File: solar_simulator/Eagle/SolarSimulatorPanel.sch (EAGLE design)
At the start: 131 parts, among them J1 DCJ0202, J2 DCJ0202

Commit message: rev 2.1 of solar simulator
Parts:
- removed R28: 220, oresat-rcl:R-US_0402-A-NOSILK
- removed U$5: AP2127, U-Diodes-AP2127-LDO:AP2127
- added C13, C14, C15: 10u, rcl:C-EUC2220K
- added TP27, TP28, TP29, TP30: TEST-POINT, Tova:TEST-POINT
- BLUE1, BLUE10, BLUE11, BLUE12, BLUE13, BLUE14, BLUE15, BLUE2, BLUE3, BLUE4, BLUE5, BLUE6, BLUE7, BLUE8: DIS (none) -> Digi-Key; DPN (none) -> XQEROY-00-0000-000000L01CT-ND; MFR (none) -> Cree; MPN (none) -> XQEROY-00-0000-000000L01
- BLUE9: DIS (none) -> Digi-Key; DPM (none) -> XQEROY-00-0000-000000L01CT-ND; MFR (none) -> Cree; MPN (none) -> XQEROY-00-0000-000000L01
- C1: value .1 u -> 100n
- C12, C2, C4, C5, C6: value .1u -> 100n
- C7, C8, C9: value .15u -> 150n; device oresat-rcl:C-EU0402-A-NOSILK -> rcl:C-EUC0805K
- GREE9, GREEN10, GREEN11, GREEN12, GREEN15, GREEN4, GREEN5, GREEN6, GREEN7, GREEN8: DIS (none) -> Digi-Key; DPN (none) -> XQEGRN-00-0000-000000D03CT-ND; MFR (none) -> Cree; MPN (none) -> XQEGRN-00-0000-000000D03
- GREEN1: DIS (none) -> Digi-Key; DPN (none) -> XQEGRN-00-0000-000000D03CT-ND; MFR (none) -> CREE; MPN (none) -> XQEGRN-00-0000-000000D03
- GREEN13: DIS (none) -> Digi-Key; DPN (none) -> XQEGRN-00-0000-000000D03CT-ND; MFR (none) -> Green; MPN (none) -> XQEGRN-00-0000-000000D03
- GREEN14, GREEN3: DIS (none) -> Digi-Key; DPN (none) -> XQEGRN-00-0000-000000D03CT-ND; MPN (none) -> XQEGRN-00-0000-000000D03
- GREEN2: DPN (none) -> XQEGRN-00-0000-000000D03CT-ND; MFR (none) -> Cree; MPN (none) -> XQEGRN-00-0000-000000D03
- J1: value DCJ0202 -> PJ-102B; device con-jack:DCJ0202 -> J-CUI-PJ102B-Barrel_Jack:PJ-102B; DIS (none) -> Digi-Key; DPN (none) -> 626-1968-ND; MFR (none) -> Conec
- J2: value DCJ0202 -> RAPC722BKZ-TH; device con-jack:DCJ0202 -> J-SwitchCraft-RAPC722BKZ-Barrel_Jack:RAPC722BKZ-TH; DIS (none) -> Digi-Key; DPN (none) -> SC3832-ND; MFR (none) -> SwitchCraft; MPN (none) -> RAPC722BKZ
- L1: DIS (none) -> Digi-Key; DPN (none) -> TE2201TR-ND; MPN (none) -> SH150S-1.02-168
- L2, L3: DIS (none) -> Digi-Key; DPN (none) -> TE2201TR-ND; MFR (none) -> Amgis; MPN (none) -> SH150S-1.02-168
- PCB1: device solarsim:ARDUINO_NANO -> U-Arduino-Nano-DevBoard:ARDUINO_NANO
- R1, R2: value 10k -> 4.7k
- R18, R19, R20: value TBD -> 300m; device oresat-rcl:R-US_0402-A-NOSILK -> rcl:R-US_R0805
- RED1, RED10, RED11, RED12, RED13, RED14, RED15, RED2, RED3, RED4, RED5, RED6, RED7, RED8, RED9: DIS (none) -> Digi-Key; DPN (none) -> XQERED-00-0000-000000701CT-ND; MFR (none) -> Cree; MPN (none) -> XQERED-00-0000-000000701
- RT1, RT2, RT3, RT4: device solarsim:NTCTHERMISTER -> R-Generic-Thermister0402:NTCTHERMISTER
- U$1, U$3: value TPS92512 -> (none); DIS (none) -> Digi-Key; DPN (none) -> 296-41002-1-ND; MFR (none) -> Texas Instruments; MPN (none) -> TPS92512DGQR
- U$2: value TPS92512 -> (none); DIS (none) -> Digi-key; DPN (none) -> 296-41002-1-ND; MFR (none) -> Texas Instruments; MPN (none) -> TPS92512DGQR
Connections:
- net N$1 renamed SDA
- net N$3 renamed SCL
- net N$32 renamed !LDAC
- net VCC renamed 12V
- removed net N$73: U$6.S, U$7.P$1
- removed net N$74: U$7.P$2, U$8.P$1
- removed net N$75: U$8.P$2, U$9.P$1
- removed net N$76: U$10.P$1, U$9.P$2
- removed net N$78: R28.1, R29.2, TP15.1, U$6.G
- removed net VCC/2: C4.1, C5.1, J2.3, R6.2, R8.2, TP12.1, U$2.VIN, U$3.VIN
- removed net VCC/3: C6.1, R10.2, U$1.VIN
- new net !RESET: PCB1.RESET, TP27.1
- new net 56V: C13.1, C14.1, C15.1, C4.1, C5.1, C6.1, J2.3, R10.2, R6.2, R8.2, TP12.1, U$1.VIN, U$2.VIN, U$3.VIN
- new net N$62: U$10.P$1, U$6.S, U$7.P$1, U$8.P$1, U$9.P$1
- new net N$84: TP30.1, U$3.PDIM
- new net N$85: TP28.1, U$2.PDIM
- new net N$86: TP29.1, U$1.PDIM
- net GND: now also C13.2, C14.2, C15.2, U$7.P$2, U$8.P$2, U$9.P$2; no longer U$5.GND
- net N$22: no longer C7.1
- net N$24: no longer C8.1
- net N$25: no longer C9.1
- net N$4: no longer TP16.1, U$5.VOUT
- net N$69: now also C9.1
- net N$70: now also C8.1
- net N$72: now also C7.1
- net N$79: now also R29.2, TP15.1, U$6.G; no longer R28.2
- net N$80: now also TP16.1, U$4.VOUTD; no longer U$5.!SHDN, U$5.VIN
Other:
- note added: "0805"
- note added: "NOTE: AREF bypassed on daughter board"
- note added: "NOTE: All resistors and capacitors are 0402 unless otherwise noted"
- note added: "NOTE: Switching Frequency is 1 MHz"
- note added: "TODO: Give Values to diode"
- note added: "TODO: Reference designator and value"
- note added: "TODO: add reference designator"
- note added: "TODO: extend board and add 4 mounting holes for solar panel. Use solar panel holes on top and bottom of board"
- moved on the sheet: C4, C5, C6, D1, D2, D3, J2, L1, L2, L3, R1, R2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

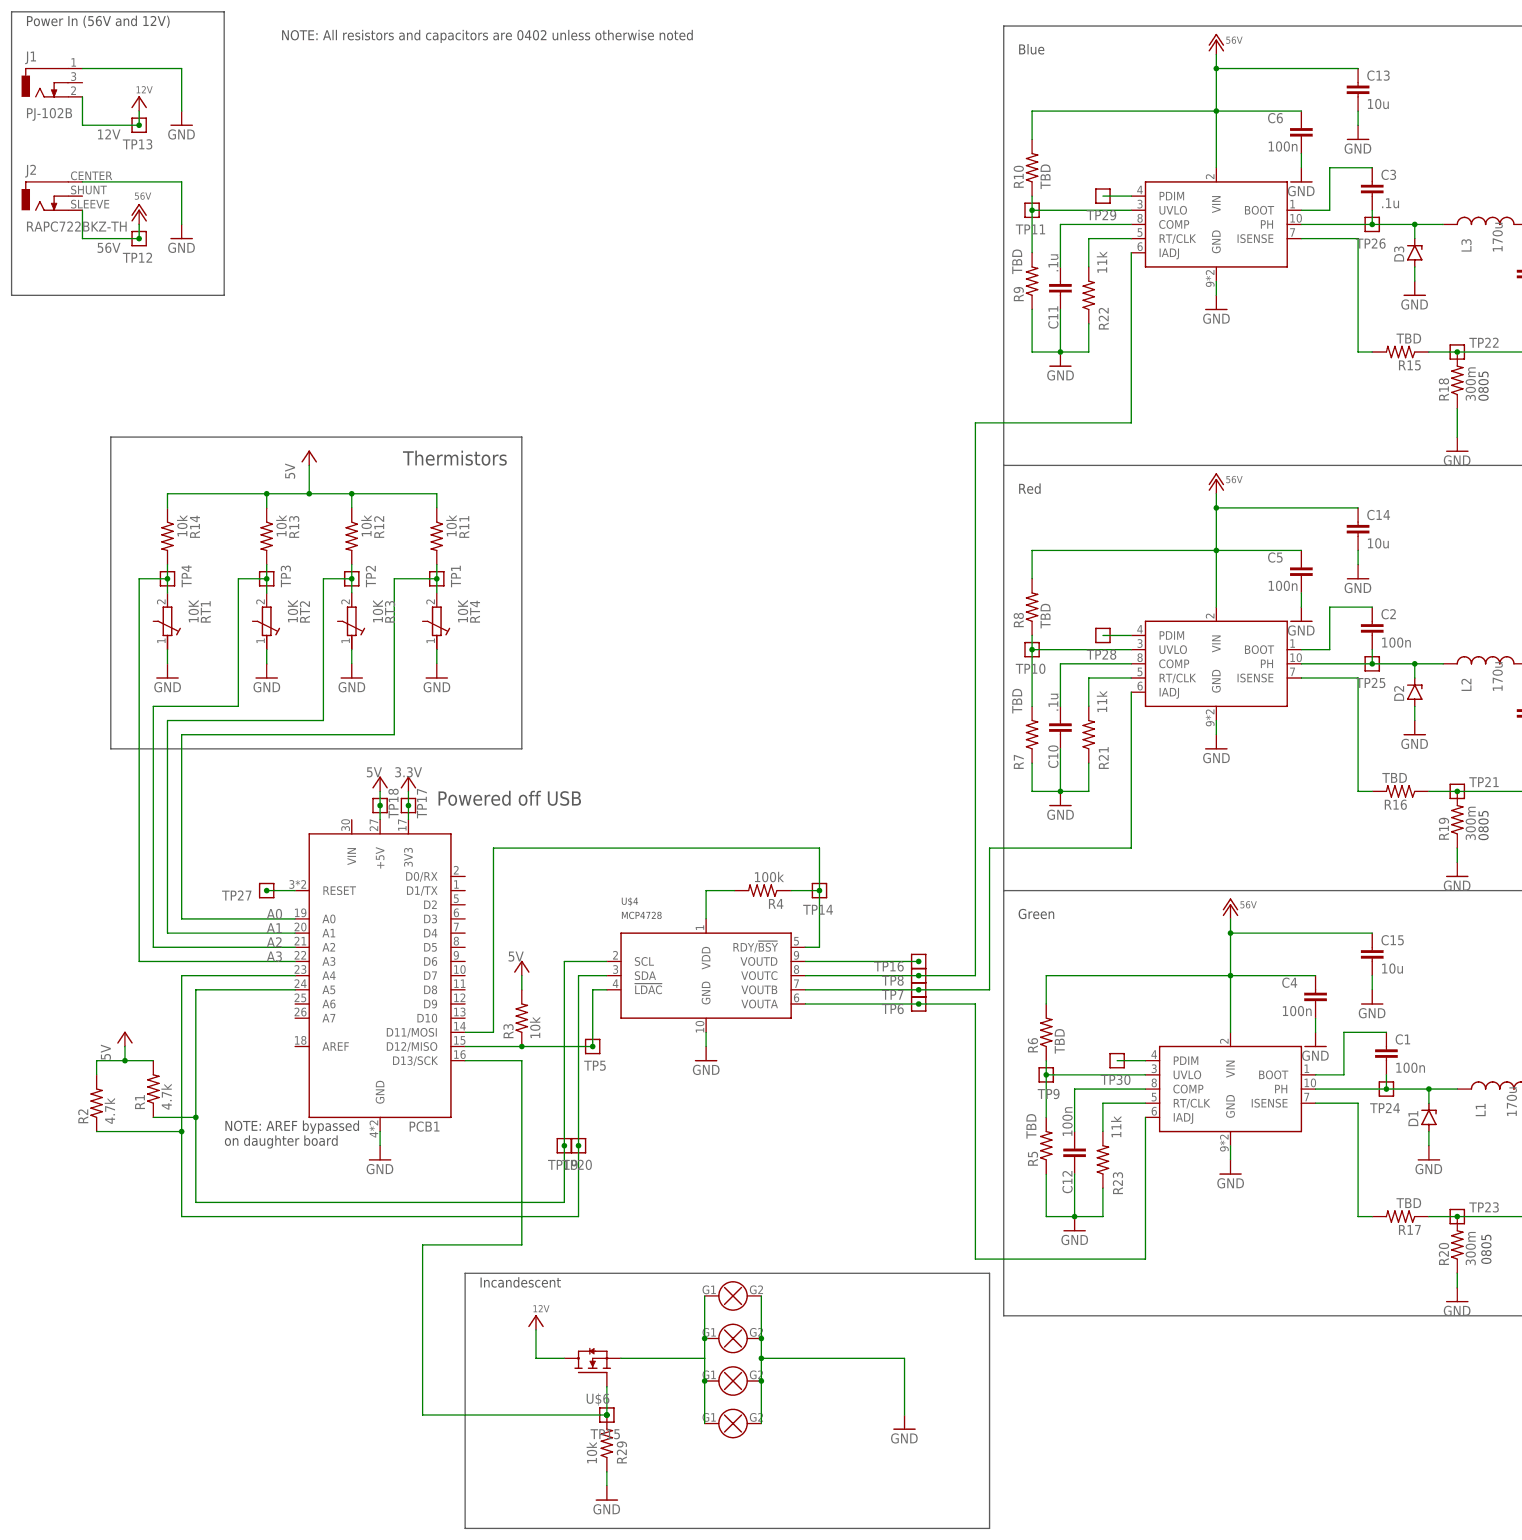
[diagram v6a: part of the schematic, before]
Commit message: revisions for solar simulator 2.0, removed outdated solarsim.lbr, new parts in oresat-eagle repo
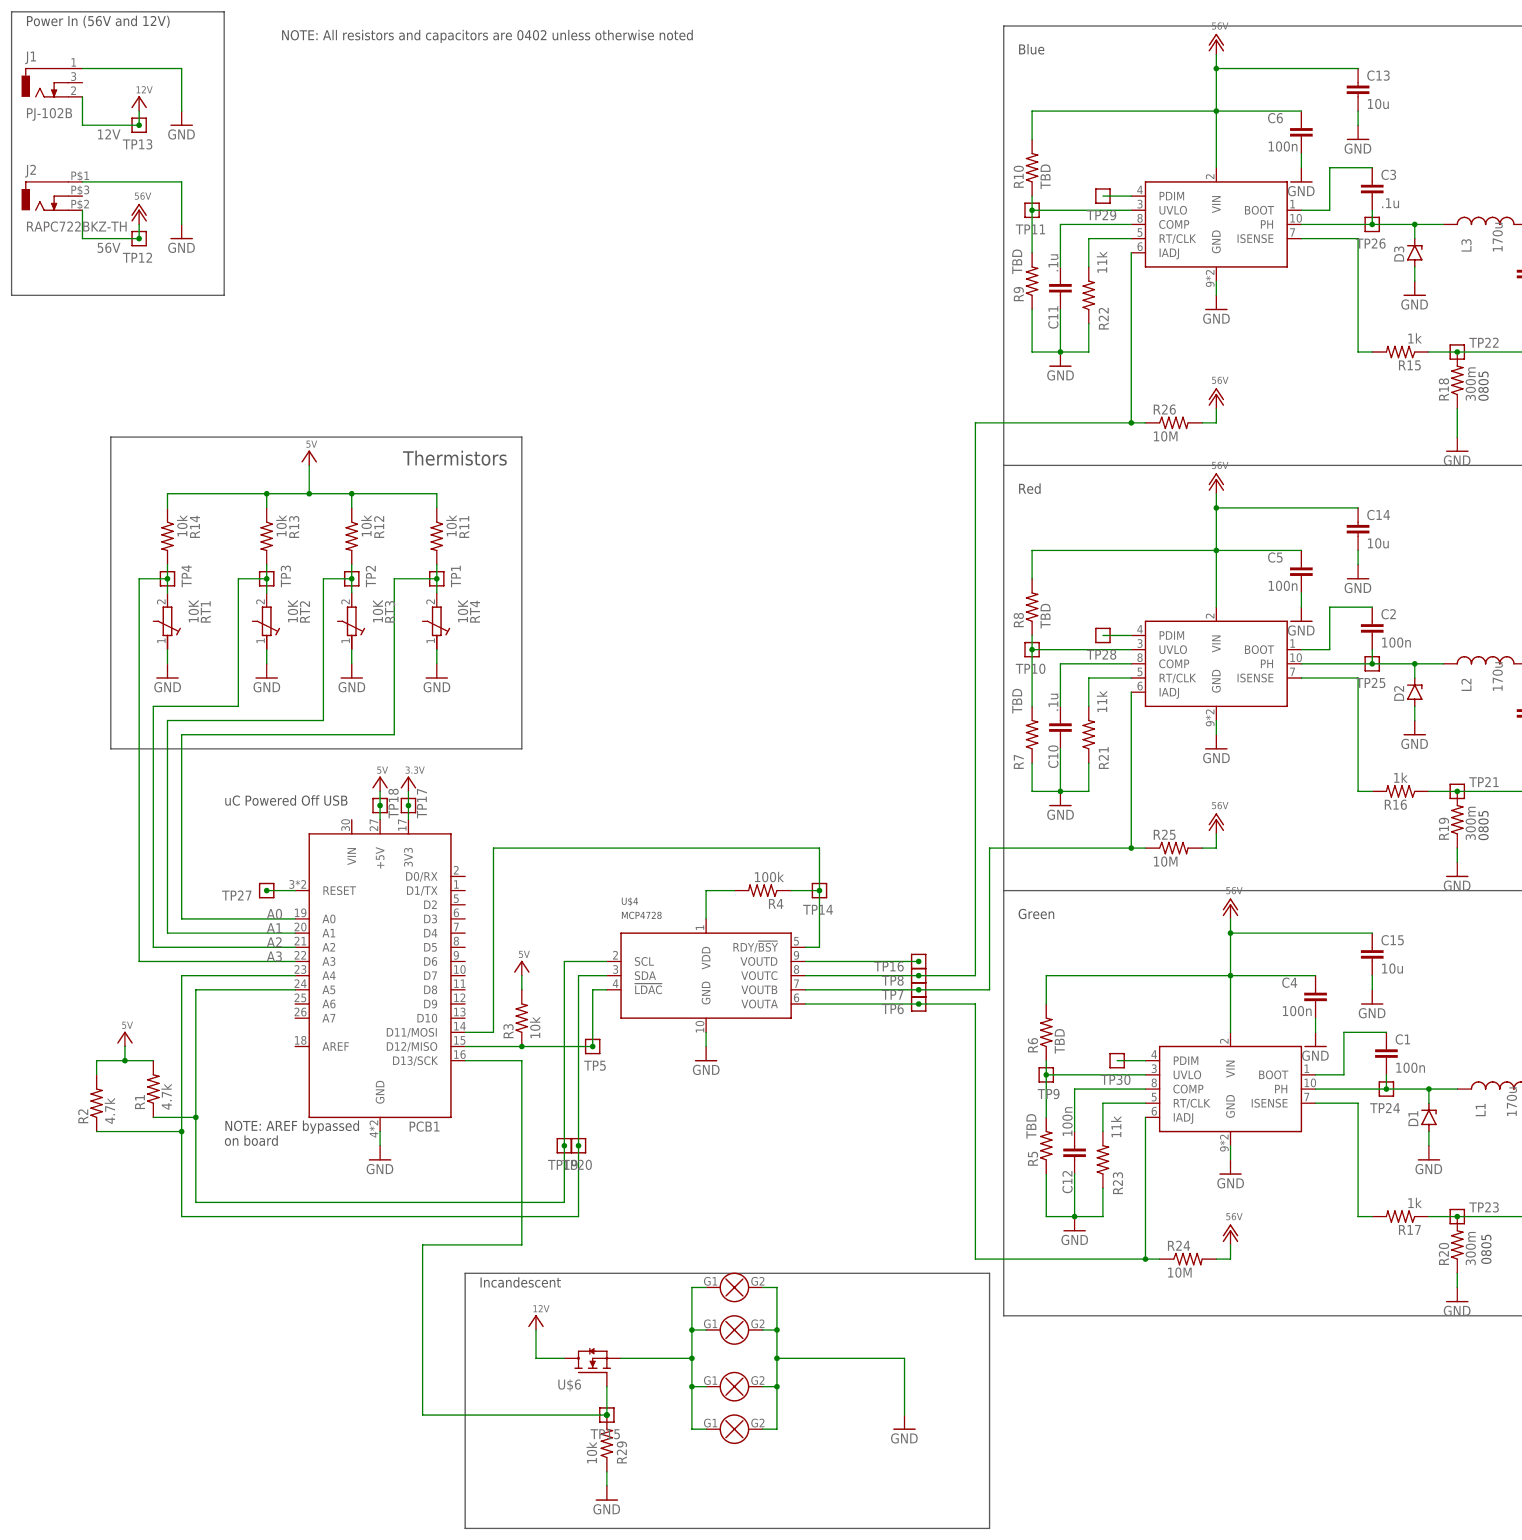
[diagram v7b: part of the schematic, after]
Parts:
- added R24, R25, R26: 10M, rcl:R-US_R0402
- R15, R16, R17: value TBD -> 1k
- U$6: MPN (none) -> DMN6068SE
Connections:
- net +3V3 renamed 3.3V
- net +5V renamed 5V
- net 56V: now also R24.2, R25.2, R26.2
- net N$18: now also R25.1
- net N$64: now also R26.1
- net N$68: now also R24.1
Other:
- note added: "NOTE: AREF bypassed on board"
- note added: "uC Powered Off USB"
- note removed: "NOTE: AREF bypassed on daughter board"
- note removed: "Powered off USB"
- note removed: "TODO: extend board and add 4 mounting holes for solar panel. Use solar panel holes on top and bottom of board"
- moved on the sheet: J2

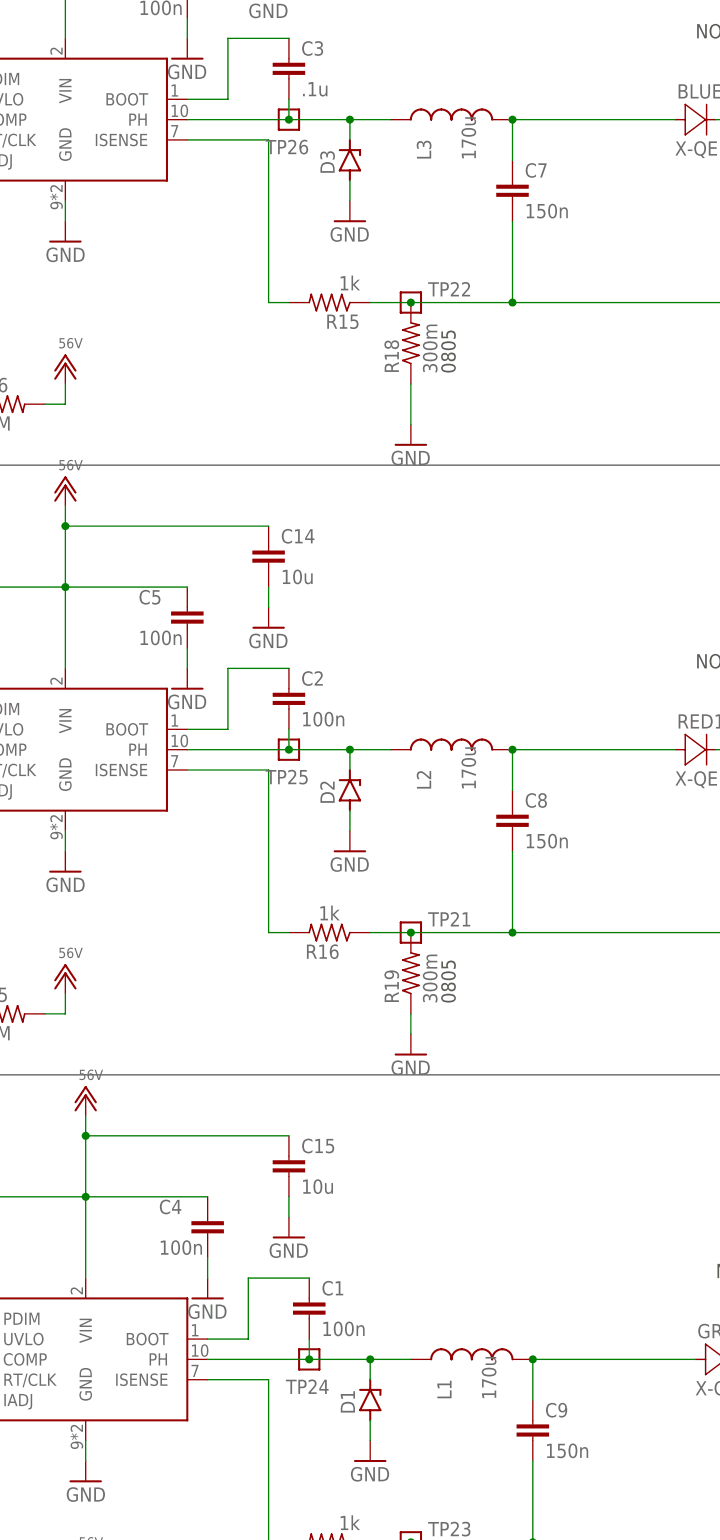
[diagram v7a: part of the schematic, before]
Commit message: silkscreen tweaks to solar simulator
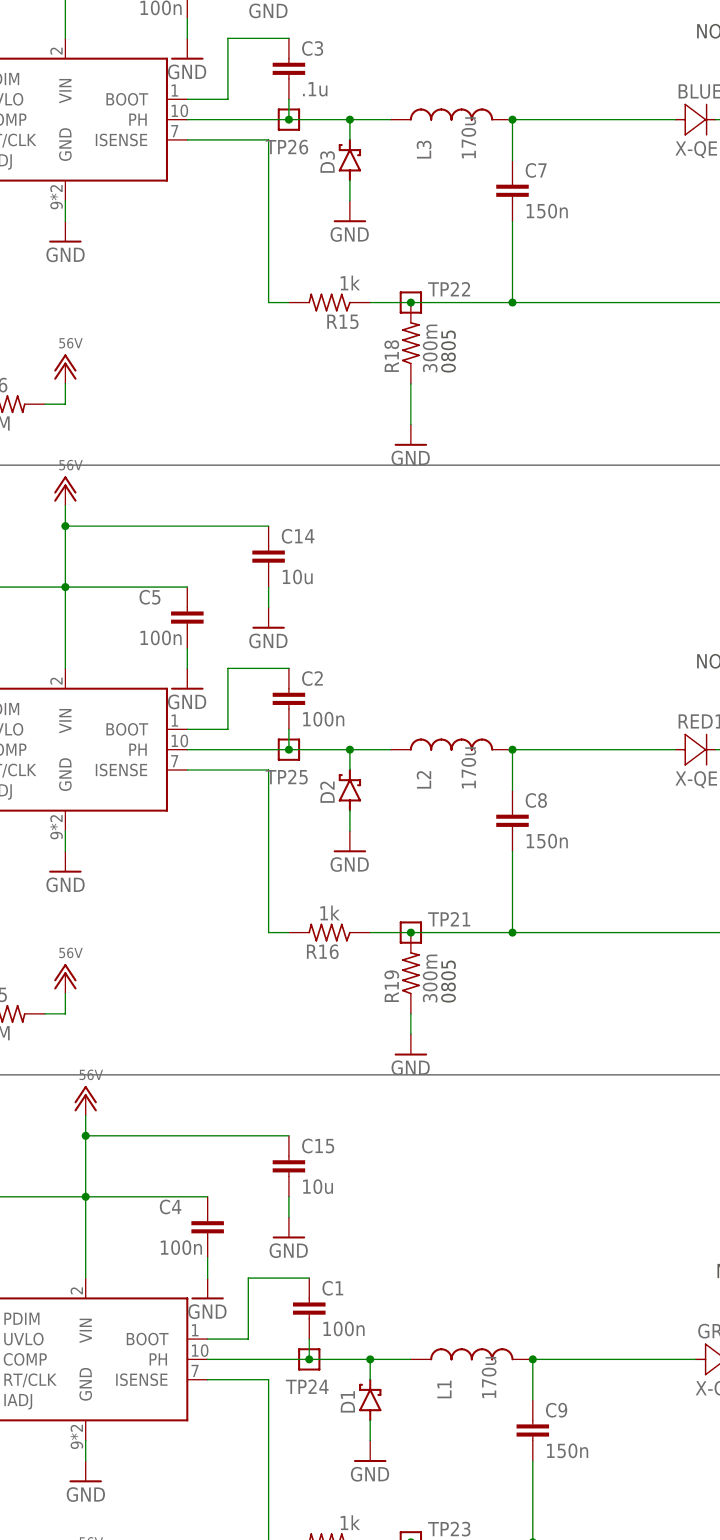
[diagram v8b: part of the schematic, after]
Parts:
- D1, D2, D3: value (none) -> D-MCC-SS2150; device diode:ZENER-DIODESMB -> D-MCC-SS2150-Schottky:D-MCC-SS2150
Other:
- note removed: "TODO: Give Values to diode"
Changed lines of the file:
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@@
 <?xml version="1.0" encoding="utf-8"?>
 <!DOCTYPE eagle SYSTEM "eagle.dtd">
-<eagle version="9.4.0">
+<eagle version="9.5.2">
 <drawing>
 <settings>
@@
 <part name="C2" library="oresat-rcl" deviceset="C-EU" device="0402-A-NOSILK" value="100n"/>
 <part name="C3" library="oresat-rcl" deviceset="C-EU" device="0402-A-NOSILK" value=".1u"/>
-<part name="D1" library="diode" library_urn="urn:adsk.eagle:library:210" deviceset="ZENER-DIODE" device="SMB" package3d_urn="urn:adsk.eagle:package:43404/2"/>
-<part name="D2" library="diode" library_urn="urn:adsk.eagle:library:210" deviceset="ZENER-DIODE" device="SMB" package3d_urn="urn:adsk.eagle:package:43404/2"/>
-<part name="D3" library="diode" library_urn="urn:adsk.eagle:library:210" deviceset="ZENER-DIODE" device="SMB" package3d_urn="urn:adsk.eagle:package:43404/2"/>
+<part name="D1" library="D-MCC-SS2150-Schottky" deviceset="D-MCC-SS2150" device=""/>
+<part name="D2" library="D-MCC-SS2150-Schottky" deviceset="D-MCC-SS2150" device=""/>
+<part name="D3" library="D-MCC-SS2150-Schottky" deviceset="D-MCC-SS2150" device=""/>
 <part name="GND1" library="supply1" library_urn="urn:adsk.eagle:library:371" deviceset="GND" device=""/>
 <part name="GND10" library="supply1" library_urn="urn:adsk.eagle:library:371" deviceset="GND" device=""/>
@@
 <text x="185.42" y="266.7" size="1.778" layer="97">Blue</text>
 <text x="142.24" y="83.82" size="1.778" layer="113">TODO: add reference designator</text>
-<text x="276.86" y="50.8" size="1.778" layer="113">TODO: Give Values to diode</text>
 <text x="210.82" y="208.28" size="1.778" layer="113">TODO: Reference designator and value</text>
 <text x="43.18" y="71.12" size="1.778" layer="97">NOTE: AREF bypassed
@@
 <instance part="D1" gate="G$1" x="259.08" y="76.2" smashed="yes" rot="R90">
 <attribute name="NAME" x="257.175" y="74.422" size="1.778" layer="95" rot="R90"/>
-<attribute name="VALUE" x="262.509" y="74.422" size="1.778" layer="96" rot="R90"/>
 </instance>
 <instance part="D2" gate="G$1" x="256.54" y="152.4" smashed="yes" rot="R90">
 <attribute name="NAME" x="254.635" y="150.622" size="1.778" layer="95" rot="R90"/>
-<attribute name="VALUE" x="259.969" y="150.622" size="1.778" layer="96" rot="R90"/>
 </instance>
 <instance part="D3" gate="G$1" x="256.54" y="231.14" smashed="yes" rot="R90">
 <attribute name="NAME" x="254.635" y="229.362" size="1.778" layer="95" rot="R90"/>
-<attribute name="VALUE" x="259.969" y="229.362" size="1.778" layer="96" rot="R90"/>
 </instance>
 <instance part="GND1" gate="1" x="259.08" y="68.58" smashed="yes">
